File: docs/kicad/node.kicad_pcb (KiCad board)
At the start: 2 copper layers, 123 x 153 mm, 15 parts, among them J1 Conn_01x01_Pin, J2 Conn_01x01_Pin, J3 Conn_01x01_Pin, J4 Conn_01x01_Pin, J5 Conn_01x01_Pin, J6 Conn_01x01_Pin, J7 Conn_01x01_Pin, J8 Conn_01x01_Pin, J9 Conn_01x08, U1 ESP32-DevKitC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

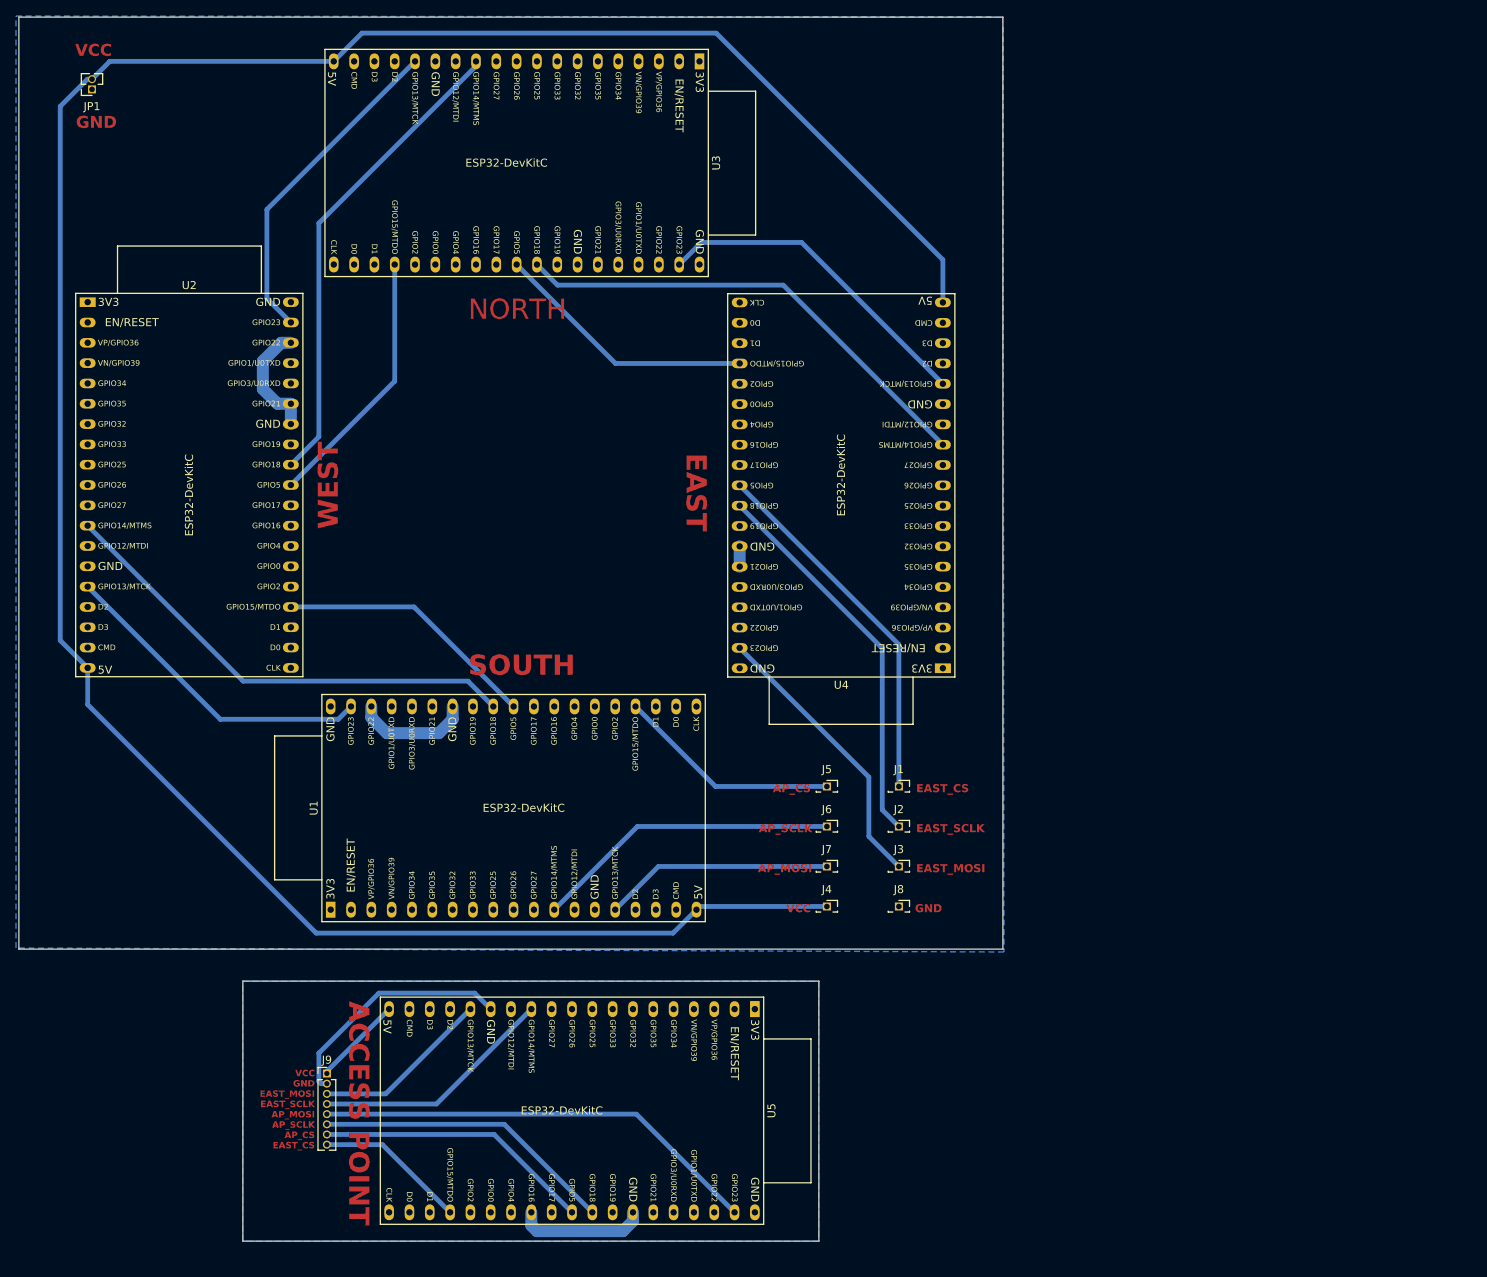
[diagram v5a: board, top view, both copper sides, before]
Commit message: used 8mm routes 1mm clearance, having some gnd islands
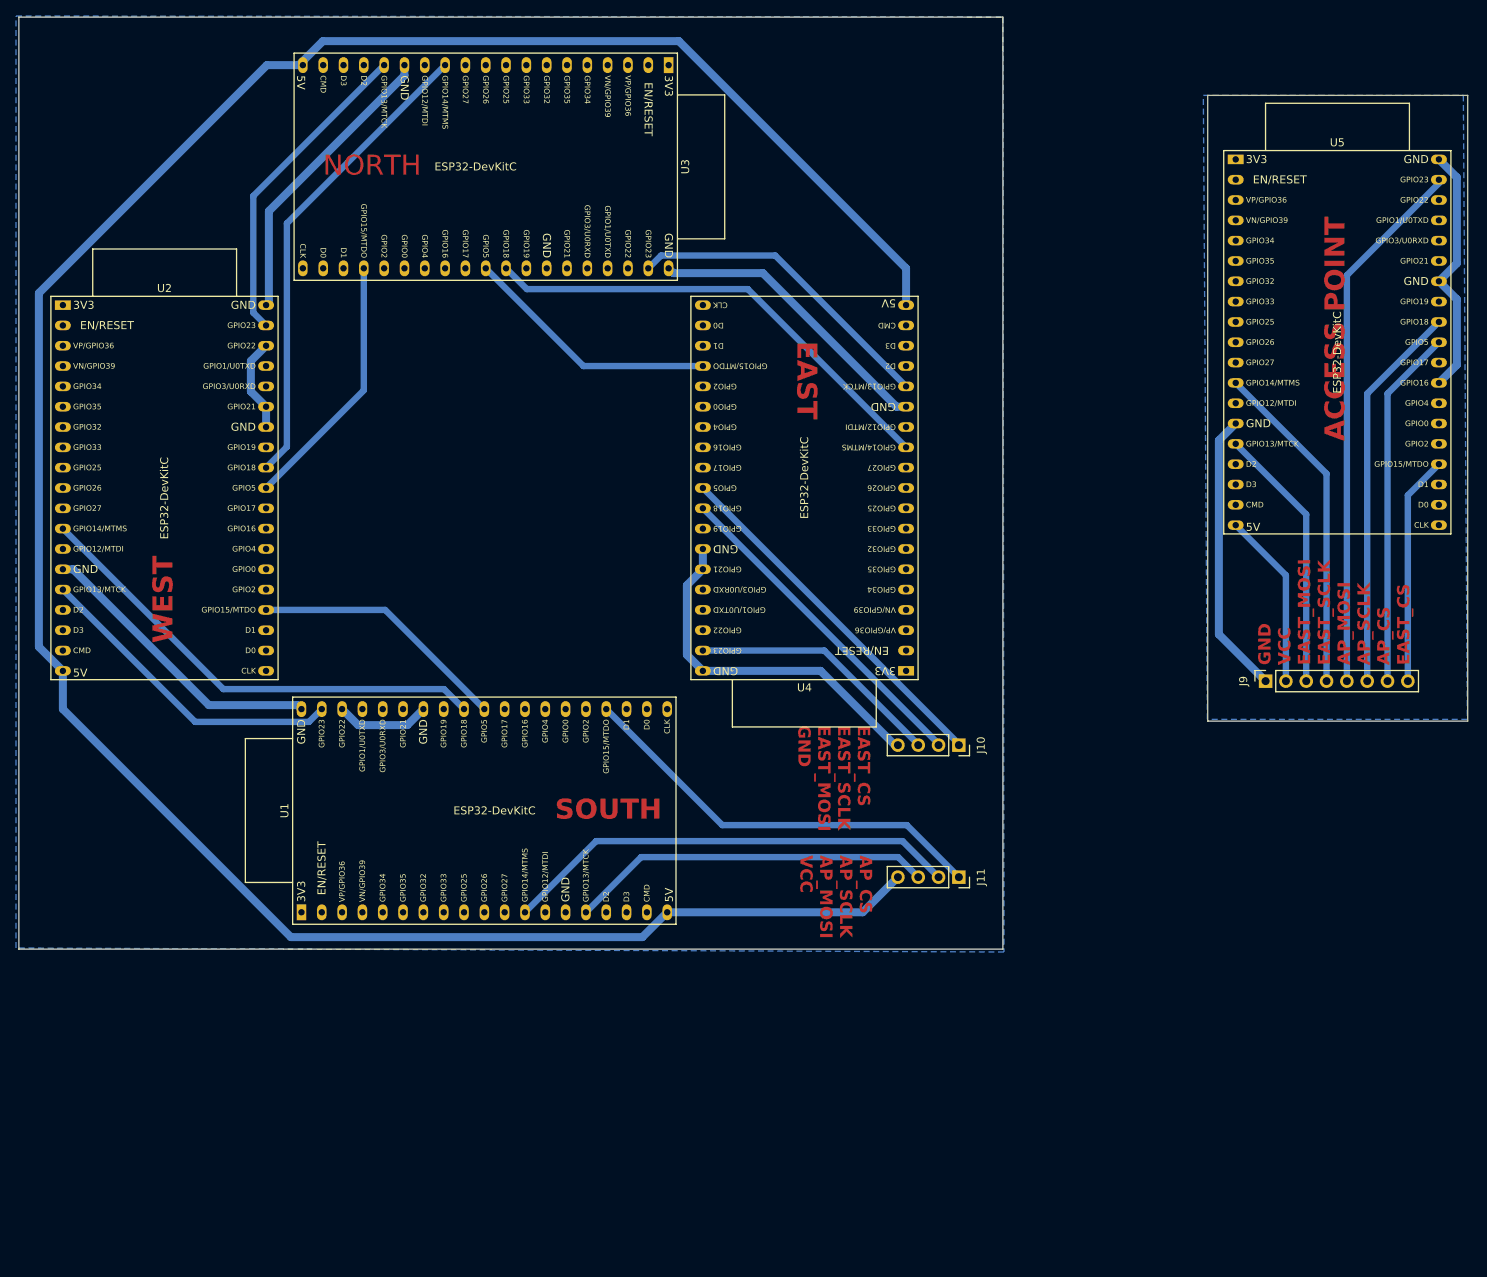
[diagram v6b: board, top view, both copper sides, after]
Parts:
- removed J1, J2, J3, J4, J5, J6, J7, J8: Conn_01x01_Pin, Connector_PinSocket_1.27mm:PinSocket_1x01_P1.27mm_Vertical
- removed JP1: Jumper_2_Open, Connector_PinSocket_1.27mm:PinSocket_1x02_P1.27mm_Vertical
- added J10: Conn_01x04_Pin, Connector_PinSocket_2.54mm:PinSocket_1x04_P2.54mm_Vertical, F.Cu at (130.0, 103.5)
- added J11: Conn_01x04_Pin, Connector_PinSocket_2.54mm:PinSocket_1x04_P2.54mm_Vertical, F.Cu at (130.0, 120.0)
- J9: footprint Connector_PinHeader_1.27mm:PinHeader_1x08_P1.27mm_Vertical -> Connector_PinSocket_2.54mm:PinSocket_1x08_P2.54mm_Vertical
- moved J9 127.2 mm to (168.3, 95.5), turned to 90 degrees
- moved U5 122.0 mm to (164.6, 30.3), turned to 0 degrees
- moved U4 4.61 mm to (123.4, 94.2)
- moved U3 3.89 mm to (93.7, 18.5)
- moved U1 3.67 mm to (47.8, 124.4)
- moved U2 3.12 mm to (18.0, 48.5)
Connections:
- J9 pad 1: /ap/VCC -> GND1
- J9 pad 2: GND1 -> /ap/VCC
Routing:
- net GND: track 32.0 -> 179.7 mm
- net /main/B5_CS: track 28.1 -> 52.8 mm
- net GND1: track 46.3 -> 67.1 mm
- net /main/B5_SCLK: track 38.4 -> 57.2 mm
- net /main/B5_MOSI: track 28.7 -> 45.4 mm
- net /ap/B4_SCLK: track 30.5 -> 42.0 mm
- net /ap/B5_MOSI: track 56.0 -> 67.4 mm
- net /ap/B4_MOSI: track 22.3 -> 33.3 mm
- net /ap/B5_SCLK: track 37.7 -> 48.6 mm
- net /ap/VCC: track 11.3 -> 22.1 mm
- net /ap/B5_CS: track 34.7 -> 45.0 mm
- net /ap/B4_CS: track 18.9 -> 28.7 mm
- net /main/B4_SCLK: track 48.3 -> 41.8 mm
- net /main/B4_MOSI: track 35.6 -> 31.9 mm
- net /main/VCC: track 313.0 -> 310.8 mm
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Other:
- board size 123 x 153 mm -> 181.1 x 116.5 mm
- board text added: "AP_CS AP_SCLK AP_MOSI VCC"
- board text added: "EAST_CS EAST_SCLK EAST_MOSI GND"
- board text added: "GND VCC EAST_MOSI EAST_SCLK AP_MOSI AP_SCLK AP_CS EAST_CS"
- board text removed: "AP_CS"
- board text removed: "AP_MOSI"
- board text removed: "AP_SCLK"
- board text removed: "EAST_CS"
- board text removed: "EAST_MOSI"
- board text removed: "EAST_SCLK"
- board text removed: "GND"
- board text removed: "VCC"
- board text removed: "VCC GND EAST_MOSI EAST_SCLK AP_MOSI AP_SCLK AP_CS EAST_CS"

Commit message: resolved all errors
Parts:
- moved J11 12.8 mm to (122.0, 130.0)
- moved J9 11.5 mm to (161.8, 105.0)
- moved U5 11.5 mm to (158.1, 39.8)
- moved J10 9.18 mm to (122.0, 108.0)
- moved U1 9.04 mm to (54.0, 131.0)
- moved U4 8.83 mm to (131.0, 98.7)
- moved U3 6.35 mm to (99.0, 22.0)
- moved U2 5.58 mm to (21.3, 53.0)
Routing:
- net /main/B4_MOSI: track 31.9 -> 16.5 mm
- net /main/B5_MOSI: track 45.4 -> 32.5 mm
- net /main/B5_SCLK: track 57.2 -> 46.0 mm
- net /main/B5_CS: track 52.8 -> 42.1 mm
- net /main/B4_SCLK: track 41.8 -> 35.5 mm
- net /main/B4_CS: track 45.4 -> 39.1 mm
- net /main/B1_MOSI: track 39.9 -> 44.8 mm
- net /main/B1_SCLK: track 59.5 -> 63.8 mm
- net /main/B1_CS: track 32.4 -> 36.8 mm
- net /main/B3_MOSI: track 39.7 -> 43.0 mm
- net /main/B2_MOSI: track 40.0 -> 42.7 mm
- net /main/B3_CS: track 32.2 -> 34.9 mm
- net /main/B3_SCLK: track 59.3 -> 62.0 mm
- net GND: track 179.7 -> 182.2 mm
- net /main/VCC: track 310.8 -> 313.2 mm
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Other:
- board size 181.1 x 116.5 mm -> 173.1 x 125 mm

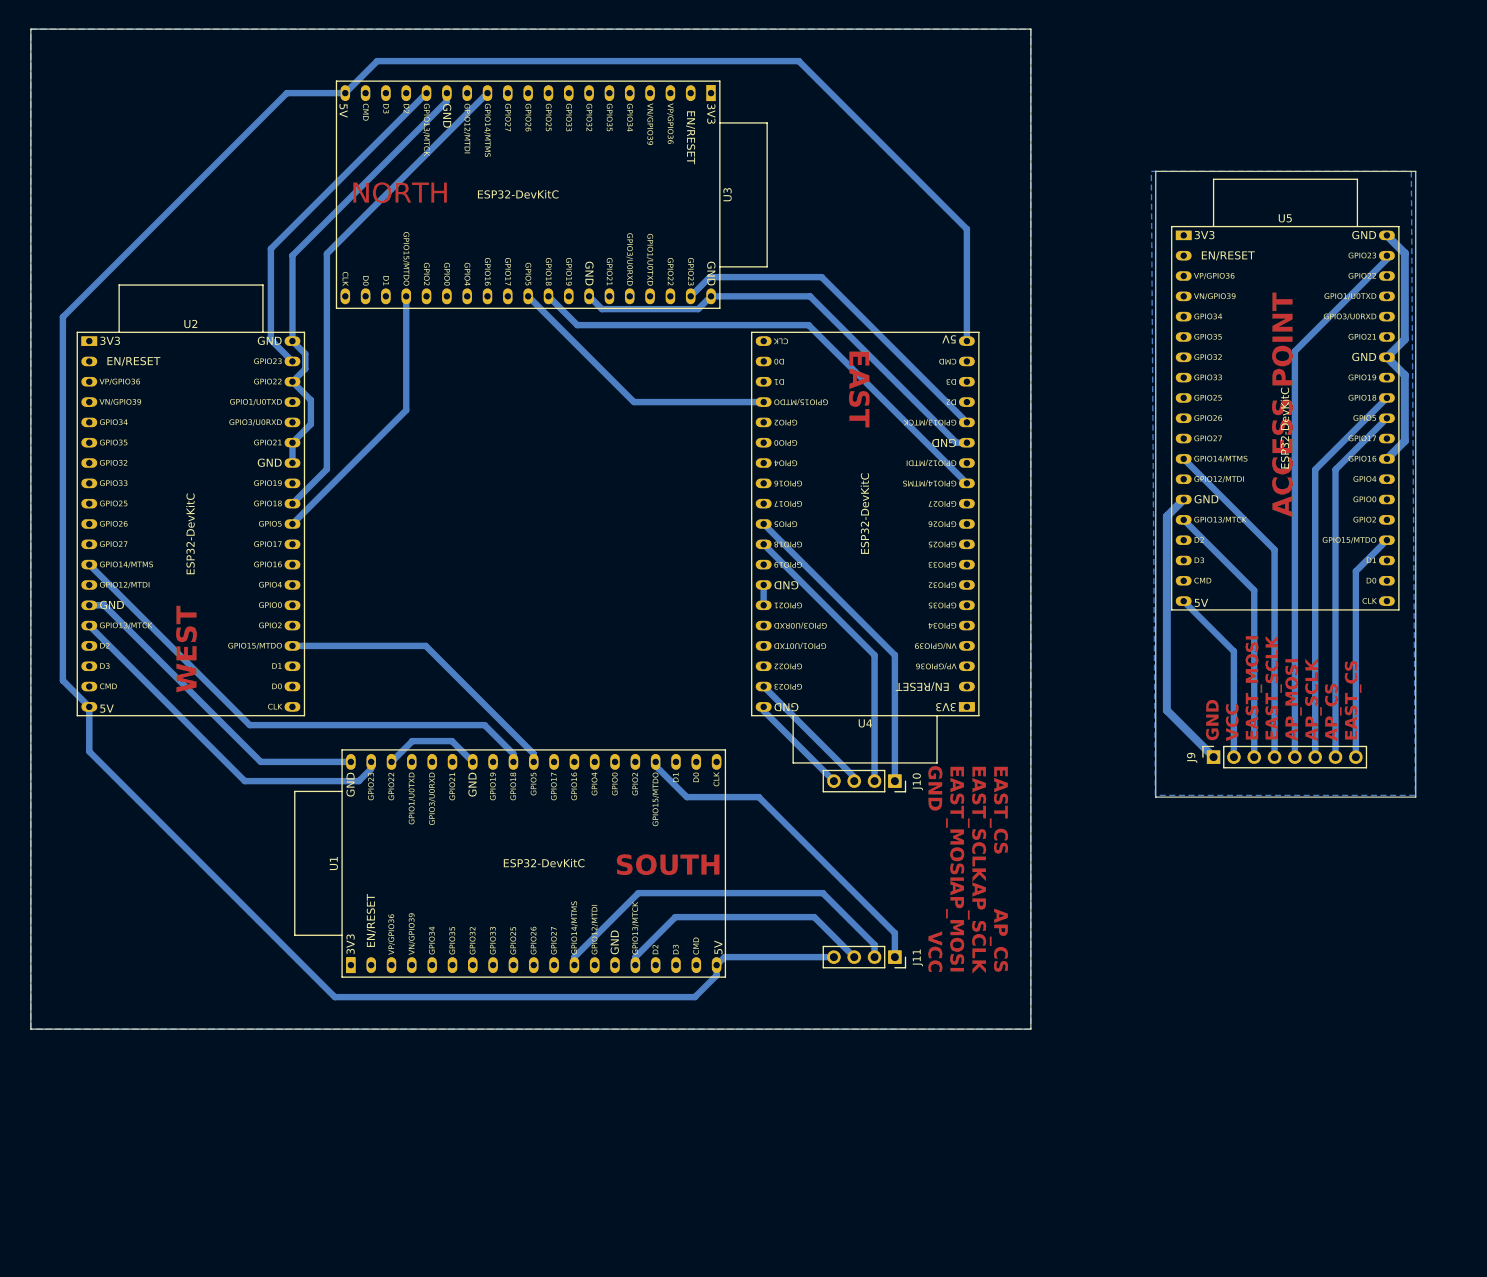
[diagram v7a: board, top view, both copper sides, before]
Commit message: use rj45 to connect
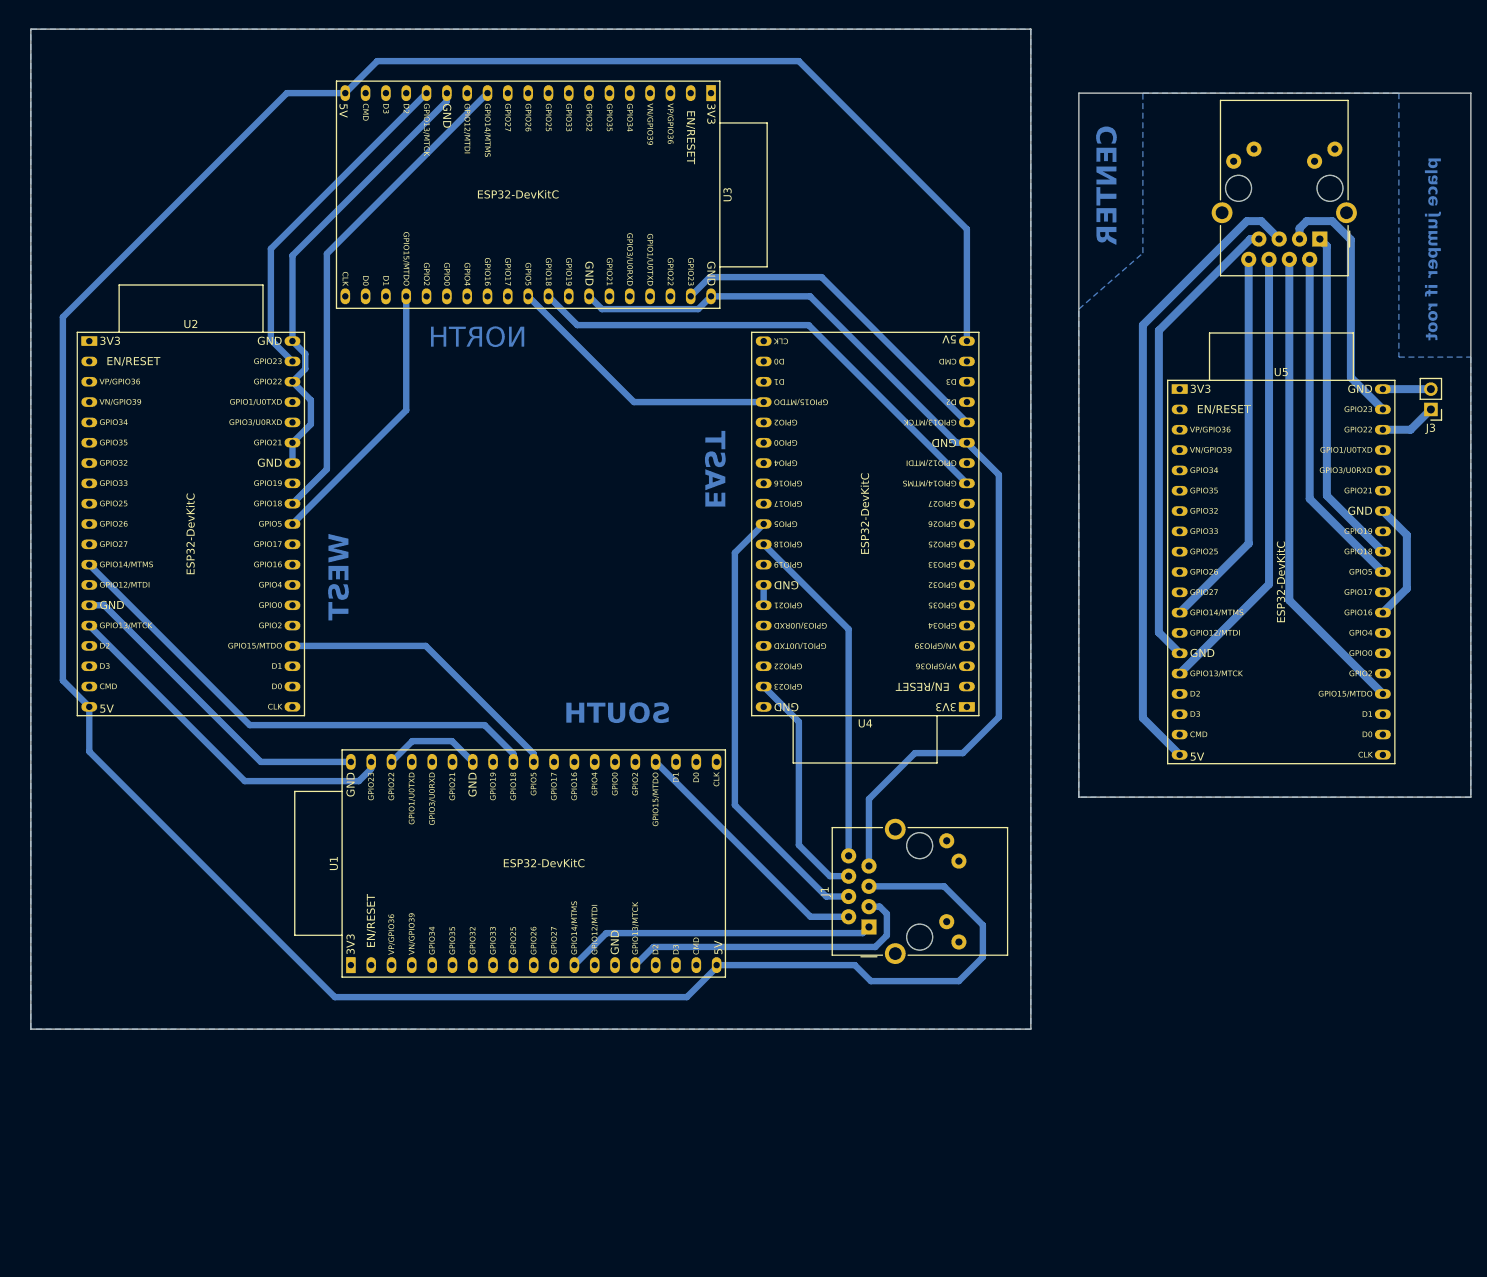
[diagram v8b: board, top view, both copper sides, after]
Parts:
- removed J10, J11: Conn_01x04_Pin, Connector_PinSocket_2.54mm:PinSocket_1x04_P2.54mm_Vertical
- removed J9: Conn_01x08, Connector_PinSocket_2.54mm:PinSocket_1x08_P2.54mm_Vertical
- added J1: RJ45, Connector_RJ:RJ45_Amphenol_RJMG1BD3B8K1ANR, F.Cu at (118.8, 126.2)
- added J2: RJ45, Connector_RJ:RJ45_Amphenol_RJMG1BD3B8K1ANR, F.Cu at (175.1, 40.2)
- added J3: Conn_01x02_Pin, Connector_PinHeader_2.54mm:PinHeader_1x02_P2.54mm_Vertical, F.Cu at (189.0, 61.5)
- moved U5 19.2 mm to (157.6, 59.0)
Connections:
- U5 pad 36: unconnected-(U5-GPIO22-Pad36) -> /ap/ROOT_PIN_2
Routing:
- net /ap/VCC: track 22.1 -> 79.0 mm
- net GND: track 182.2 -> 234.1 mm
- net /main/VCC: track 313.2 -> 353.2 mm
- net /ap/B5_MOSI: track 67.4 -> 32.0 mm
- net /ap/B4_CS: track 28.7 -> 59.2 mm
- net /ap/B4_MOSI: track 33.3 -> 56.4 mm
- net /main/B4_CS: track 39.1 -> 55.6 mm
- net /main/B4_MOSI: track 16.5 -> 29.5 mm
- net GND1: track 67.1 -> 79.8 mm
- net /main/B5_CS: track 42.1 -> 32.1 mm
- net /main/B4_SCLK: track 35.5 -> 43.3 mm
- net /main/B5_SCLK: track 46.0 -> 38.8 mm
- net /ap/ROOT_PIN_2: track 0.00 -> 7.05 mm
- net /ap/B5_SCLK: track 48.6 -> 42.3 mm
- net /main/B5_MOSI: track 32.5 -> 38.3 mm
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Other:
- board size 173.1 x 125 mm -> 180 x 125 mm
- board text added: "CENTER"
- board text added: "place jumper if root"
- board text removed: "ACCESS POINT"
- board text removed: "AP_CS AP_SCLK AP_MOSI VCC"
- board text removed: "EAST_CS EAST_SCLK EAST_MOSI GND"
- board text removed: "GND VCC EAST_MOSI EAST_SCLK AP_MOSI AP_SCLK AP_CS EAST_CS"
